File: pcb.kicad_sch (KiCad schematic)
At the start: 4 parts

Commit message: imprv to layout
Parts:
- H1, H2, H3, H4: footprint (none) -> MountingHole:MountingHole_3.2mm_M3_DIN965_Pad
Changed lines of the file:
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@@
 			)
 		)
-		(property "Footprint" ""
+		(property "Footprint" "MountingHole:MountingHole_3.2mm_M3_DIN965_Pad"
 			(at 140.97 101.6 0)
 			(effects
@@
 		)
 		(property "Supplier_2 P/N" ""
+			(at 140.97 101.6 0)
+			(effects
+				(font
+					(size 1.27 1.27)
+				)
+				(hide yes)
+			)
+		)
+		(property "Supplier_1" ""
+			(at 140.97 101.6 0)
+			(effects
+				(font
+					(size 1.27 1.27)
+				)
+				(hide yes)
+			)
+		)
+		(property "Supplier_1 P/N" ""
+			(at 140.97 101.6 0)
+			(effects
+				(font
+					(size 1.27 1.27)
+				)
+				(hide yes)
+			)
+		)
+		(property "Supplier_1 Price @ Qty" ""
+			(at 140.97 101.6 0)
+			(effects
+				(font
+					(size 1.27 1.27)
+				)
+				(hide yes)
+			)
+		)
+		(property "Supplier_1 Unit Price" ""
 			(at 140.97 101.6 0)
 			(effects
@@
 			)
 		)
-		(property "Footprint" ""
+		(property "Footprint" "MountingHole:MountingHole_3.2mm_M3_DIN965_Pad"
 			(at 140.97 63.5 0)
 			(effects
@@
 		)
 		(property "Supplier_2 P/N" ""
+			(at 140.97 63.5 0)
+			(effects
+				(font
+					(size 1.27 1.27)
+				)
+				(hide yes)
+			)
+		)
+		(property "Supplier_1" ""
+			(at 140.97 63.5 0)
+			(effects
+				(font
+					(size 1.27 1.27)
+				)
+				(hide yes)
+			)
+		)
+		(property "Supplier_1 P/N" ""
+			(at 140.97 63.5 0)
+			(effects
+				(font
+					(size 1.27 1.27)
+				)
+				(hide yes)
+			)
+		)
+		(property "Supplier_1 Price @ Qty" ""
+			(at 140.97 63.5 0)
+			(effects
+				(font
+					(size 1.27 1.27)
+				)
+				(hide yes)
+			)
+		)
+		(property "Supplier_1 Unit Price" ""
 			(at 140.97 63.5 0)
 			(effects
@@
 			)
 		)
-		(property "Footprint" ""
+		(property "Footprint" "MountingHole:MountingHole_3.2mm_M3_DIN965_Pad"
 			(at 76.2 63.5 0)
 			(effects
@@
 		)
 		(property "Supplier_2 P/N" ""
+			(at 76.2 63.5 0)
+			(effects
+				(font
+					(size 1.27 1.27)
+				)
+				(hide yes)
+			)
+		)
+		(property "Supplier_1" ""
+			(at 76.2 63.5 0)
+			(effects
+				(font
+					(size 1.27 1.27)
+				)
+				(hide yes)
+			)
+		)
+		(property "Supplier_1 P/N" ""
+			(at 76.2 63.5 0)
+			(effects
+				(font
+					(size 1.27 1.27)
+				)
+				(hide yes)
+			)
+		)
+		(property "Supplier_1 Price @ Qty" ""
+			(at 76.2 63.5 0)
+			(effects
+				(font
+					(size 1.27 1.27)
+				)
+				(hide yes)
+			)
+		)
+		(property "Supplier_1 Unit Price" ""
 			(at 76.2 63.5 0)
 			(effects
@@
 			)
 		)
-		(property "Footprint" ""
+		(property "Footprint" "MountingHole:MountingHole_3.2mm_M3_DIN965_Pad"
 			(at 76.2 102.87 0)
 			(effects
@@
 			(at 76.2 102.87 0)
 			(effects
+				(font
+					(size 1.27 1.27)
+				)
+				(hide yes)
+			)
+		)
+		(property "Supplier_1" ""
+			(at 76.2 102.87 0)
+			(effects
+				(font
+					(size 1.27 1.27)
+				)
+				(hide yes)
+			)
+		)
+		(property "Supplier_1 P/N" ""
+			(at 76.2 102.87 0)
+			(effects
+				(font
+					(size 1.27 1.27)
+				)
+				(hide yes)
+			)
+		)
+		(property "Supplier_1 Price @ Qty" ""
+			(at 76.2 102.87 0)
+			(effects
+				(font
+					(size 1.27 1.27)
+				)
+				(hide yes)
+			)
+		)
+		(property "Supplier_1 Unit Price" ""
+			(at 76.2 102.87 0)
+			(effects

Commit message: Touching up layout
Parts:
- H1, H4: footprint MountingHole:MountingHole_3.2mm_M3_DIN965_Pad -> MountingHole:MountingHole_3.2mm_M3_Pad
- H2: renamed from H3; footprint MountingHole:MountingHole_3.2mm_M3_DIN965_Pad -> MountingHole:MountingHole_3.2mm_M3_Pad
- H3: renamed from H2; footprint MountingHole:MountingHole_3.2mm_M3_DIN965_Pad -> MountingHole:MountingHole_3.2mm_M3_Pad
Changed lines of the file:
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@@
 			)
 		)
-		(property "Footprint" "MountingHole:MountingHole_3.2mm_M3_DIN965_Pad"
+		(property "Footprint" "MountingHole:MountingHole_3.2mm_M3_Pad"
 			(at 140.97 101.6 0)
 			(effects
@@
 		(dnp no)
 		(fields_autoplaced yes)
-		(property "Reference" "H2"
+		(property "Reference" "H3"
 			(at 143.51 62.2299 0)
 			(effects
@@
 			)
 		)
-		(property "Footprint" "MountingHole:MountingHole_3.2mm_M3_DIN965_Pad"
+		(property "Footprint" "MountingHole:MountingHole_3.2mm_M3_Pad"
 			(at 140.97 63.5 0)
 			(effects
@@
 			(project ""
 				(path "/30b0ade0-bb43-474b-8aae-09f32d71430b/66b59111-040b-4743-892c-9a732383e43f"
-					(reference "H2")
+					(reference "H3")
 					(unit 1)
 				)
@@
 			)
 		)
-		(property "Footprint" "MountingHole:MountingHole_3.2mm_M3_DIN965_Pad"
+		(property "Footprint" "MountingHole:MountingHole_3.2mm_M3_Pad"
 			(at 76.2 63.5 0)
 			(effects
@@
 		(dnp no)
 		(fields_autoplaced yes)
-		(property "Reference" "H3"
+		(property "Reference" "H2"
 			(at 78.74 101.5999 0)
 			(effects
@@
 			)
 		)
-		(property "Footprint" "MountingHole:MountingHole_3.2mm_M3_DIN965_Pad"
+		(property "Footprint" "MountingHole:MountingHole_3.2mm_M3_Pad"
 			(at 76.2 102.87 0)
 			(effects
@@
 			(project ""
 				(path "/30b0ade0-bb43-474b-8aae-09f32d71430b/66b59111-040b-4743-892c-9a732383e43f"
-					(reference "H3")
+					(reference "H2")
 					(unit 1)
 				)

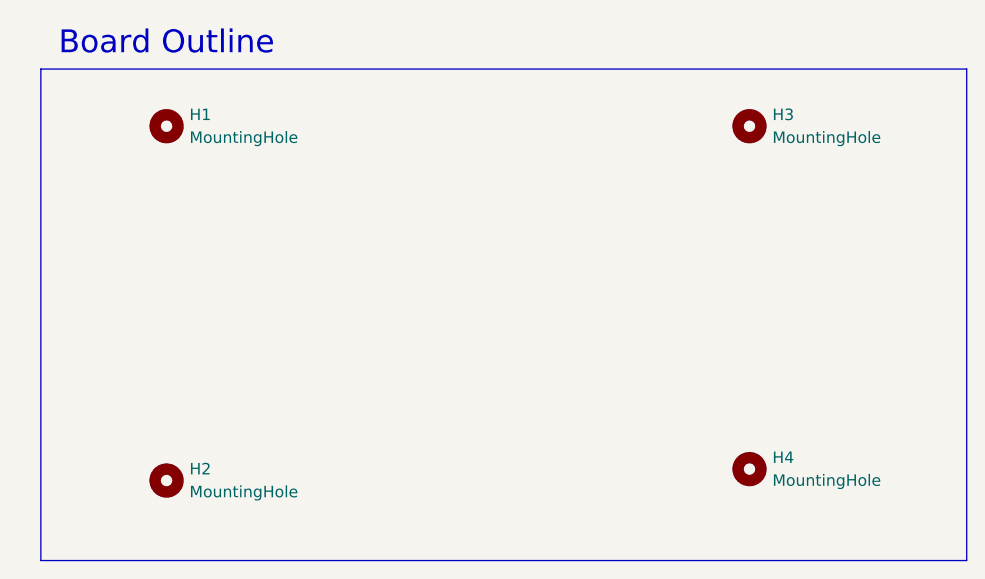
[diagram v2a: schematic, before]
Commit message: Adding in voltage divider for signal and layout and prod files
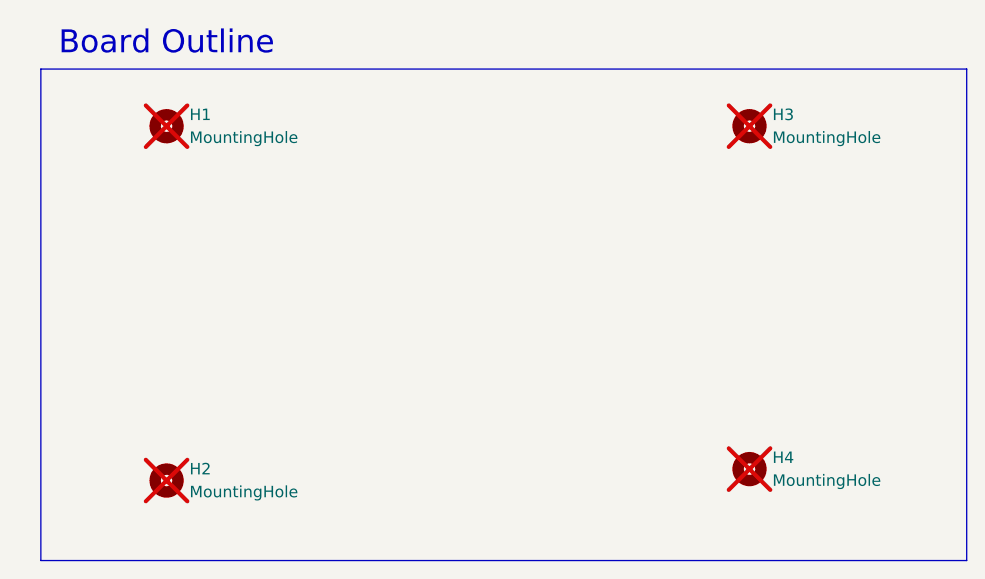
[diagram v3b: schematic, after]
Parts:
- H1, H2, H3, H4: now not fitted
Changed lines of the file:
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@@
 		(at 140.97 101.6 0)
 		(unit 1)
-		(exclude_from_sim no)
+		(exclude_from_sim yes)
 		(in_bom no)
-		(on_board yes)
-		(dnp no)
+		(on_board no)
+		(dnp yes)
 		(fields_autoplaced yes)
 		(property "Reference" "H4"
@@
 		(at 140.97 63.5 0)
 		(unit 1)
-		(exclude_from_sim no)
+		(exclude_from_sim yes)
 		(in_bom no)
-		(on_board yes)
-		(dnp no)
+		(on_board no)
+		(dnp yes)
 		(fields_autoplaced yes)
 		(property "Reference" "H3"
@@
 		(at 76.2 63.5 0)
 		(unit 1)
-		(exclude_from_sim no)
+		(exclude_from_sim yes)
 		(in_bom no)
-		(on_board yes)
-		(dnp no)
+		(on_board no)
+		(dnp yes)
 		(fields_autoplaced yes)
 		(property "Reference" "H1"
@@
 		(at 76.2 102.87 0)
 		(unit 1)
-		(exclude_from_sim no)
+		(exclude_from_sim yes)
 		(in_bom no)
-		(on_board yes)
-		(dnp no)
+		(on_board no)
+		(dnp yes)
 		(fields_autoplaced yes)
 		(property "Reference" "H2"
